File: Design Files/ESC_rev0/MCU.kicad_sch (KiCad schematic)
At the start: 0 parts

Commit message: update2
MCU sch
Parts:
- added C1, C13, C14, C2, C3, C4, C5: C, symbol Device:C
- added C10, C9: 2u2, symbol Device:C
- added C11, C15, C16, C17, C6: 100n, symbol Device:C
- added C12: 1u, symbol Device:C
- added C7: 10u, symbol Device:C
- added C8: 100nF, symbol Device:C
- added D1: LED, symbol Device:LED
- added D2: LED_G, symbol Device:LED
- added D3: LED_R, symbol Device:LED
- added FB1: FerriteBead, symbol Device:FerriteBead
- added J1: Conn_01x06, symbol Connector_Generic:Conn_01x06
- added J2: Conn_01x03, symbol Connector_Generic:Conn_01x03
- added J4: Conn_01x08, symbol Connector_Generic:Conn_01x08
- added R1: 0R, symbol Device:R
- added R10, R7, R8: 2k2, symbol Device:R
- added R2, R3: R, symbol Device:R
- added R4: 1K, symbol Device:R
- added R5, R6: 1k, symbol Device:R
- added R9: 39k, symbol Device:R
- added SW1: SW_DIP_x01, symbol Switch:SW_DIP_x01
- added TH1: 10k, symbol Device:Thermistor_NTC
- added U1: STM32F405RGTx, Package_QFP:LQFP-64_10x10mm_P0.5mm, symbol MCU_ST_STM32F4:STM32F405RGTx
- added Y1: Crystal, symbol Device:Crystal
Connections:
- new net: C13.2, R2.1, Y1.2
- new net: C11.1, C12.1, FB1.1, U1.13 (VDDA)
- new net: D3.2 (A), R6.1
- new net: D2.2 (A), R5.1
- new net: C10.1, U1.31 (VCAP_1)
- new net: J2.3 (Pin_3), R7.2
- new net: R2.2, U1.5 (PH0)
- new net: C14.2, R3.1, Y1.1
- new net: R3.2, U1.6 (PH1)
- new net: D1.2 (A), R4.1
- new net: R1.2, U1.60 (BOOT0)
- new net: C9.1, U1.47 (VCAP_2)
- new net +3V3: C1.1, C16.1, C2.1, C3.1, C4.1, C5.1, C6.1, C7.1, FB1.2, J1.1 (Pin_1), J4.2 (Pin_2), R1.1, R4.2, TH1.1, U1.1 (VBAT), U1.19 (VDD), U1.32 (VDD), U1.48 (VDD), U1.64 (VDD)
- new net +5V: J2.1 (Pin_1), J4.1 (Pin_1)
- new net +VDC: R9.2
- new net ADC_TEMP: R8.2, TH1.2, U1.17 (PA3)
- new net AN_IN: C17.1, R10.2, R9.1, U1.10 (PC2)
- new net BR_S01: U1.27 (PB1)
- new net BR_S02: U1.26 (PB0)
- new net CAN_RX: U1.61 (PB8)
- new net CAN_TX: U1.62 (PB9)
- new net DC_CAL: U1.33 (PB12)
- new net EN_GATE: U1.51 (PC10)
- new net FAULT: U1.53 (PC12)
- new net GND: C1.2, C10.2, C11.2, C12.2, C13.1, C14.1, C15.2, C16.2, C17.2, C2.2, C3.2, C4.2, C5.2, C6.2, C7.2, C8.2, C9.2, D1.1 (K), D2.1 (K), D3.1 (K), J1.3 (Pin_3), J2.2 (Pin_2), J4.3 (Pin_3), J4.8 (Pin_8), R10.1, R8.1, SW1.1, U1.12 (VSSA), U1.18 (VSS), U1.63 (VSS)
- new net H1: U1.43 (PA10)
- new net H2: U1.42 (PA9)
- new net H3: U1.41 (PA8)
- new net HALL_1: U1.58 (PB6)
- new net HALL_2: U1.59 (PB7)
- new net HALL_3: U1.52 (PC11)
- new net L1: U1.36 (PB15)
- new net L2: U1.35 (PB14)
- new net L3: U1.34 (PB13)
- new net LED_GREEN: R5.2, U1.24 (PC4)
- new net LED_RED: R6.2, U1.25 (PC5)
- new net MISO_ADC_EXT2: J4.7 (Pin_7), U1.22 (PA6)
- new net NRST: C8.1, J1.5 (Pin_5), SW1.2, U1.7 (NRST)
- new net RX_SCL_MOSI: J4.6 (Pin_6), U1.23 (PA7), U1.29 (PB10), U1.38 (PC7)
- new net SCK_ADC_EXT: J4.4 (Pin_4), U1.21 (PA5)
- new net SENS1: U1.16 (PA2)
- new net SENS2: U1.15 (PA1)
- new net SENS3: U1.14 (PA0)
- new net SERVO: C15.1, R7.1, U1.57 (PB5)
- new net SWCLK: J1.2 (Pin_2), U1.49 (PA14)
- new net SWDIO: J1.4 (Pin_4), U1.46 (PA13)
- new net TEMP_MOTOR: U1.8 (PC0)
- new net TX_SDA_NSS: J4.5 (Pin_5), U1.20 (PA4), U1.30 (PB11), U1.37 (PC6)
- new net USB_DM: U1.44 (PA11)
- new net USB_DP: U1.45 (PA12)
- no-connect marks 0 -> 13
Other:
- note added: "${TITLE}"
- note added: "100nF decoupling ceramic capacitors"
- note added: "AN_IN = VDC*0.0534 AN_IN = 3.204@60V"
- note added: "COMMUNICATION"
- note added: "NTC"
- note added: "PROGRAMMING / DEBUG"
- note added: "SERVO"
- note added: "Substitute with 100R if used as servo output"
- note added: "VOLTAGE_DIVIDER"
- note added: "internally pulled-up"
- title: (none) -> Microcontroller Unit

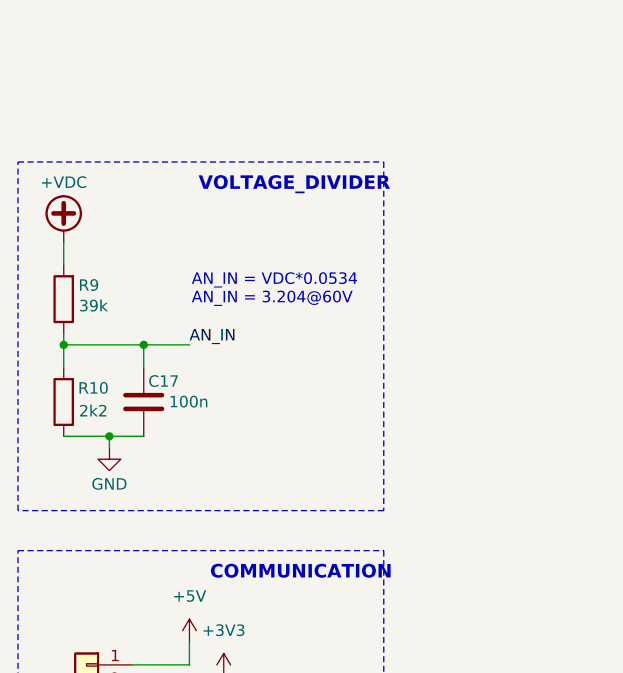
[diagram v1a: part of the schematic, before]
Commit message: update 8
conclusion of mosfets and input protection; can almost concluded
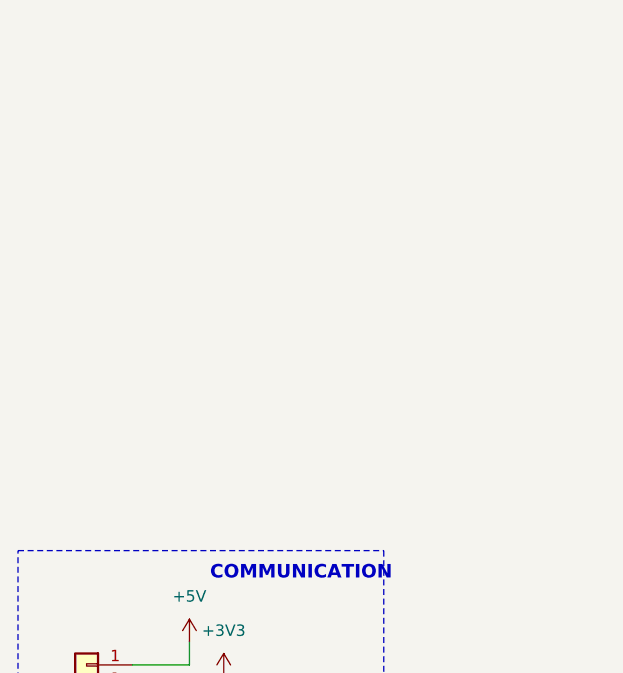
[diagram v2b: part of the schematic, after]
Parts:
- removed C17: 100n, symbol Device:C
- removed R10: 2k2, symbol Device:R
- removed R9: 39k, symbol Device:R
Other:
- note removed: "AN_IN = VDC*0.0534 AN_IN = 3.204@60V"
- note removed: "VOLTAGE_DIVIDER"

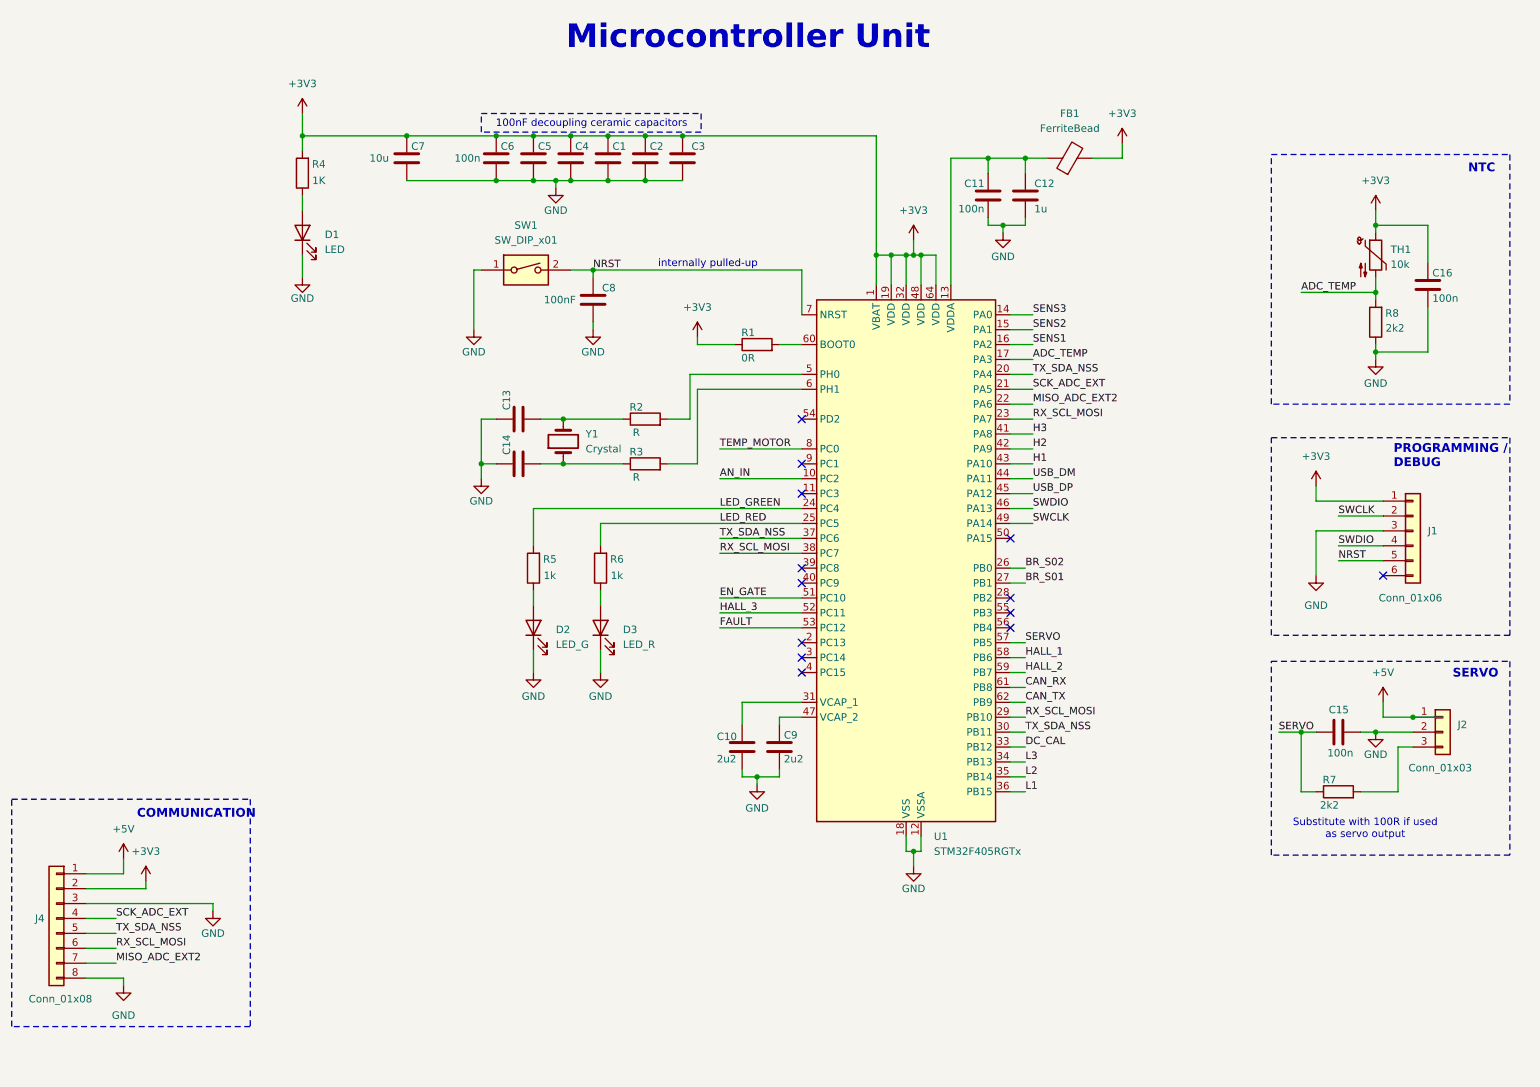
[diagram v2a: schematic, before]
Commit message: update10
modifications to root page, completion of pages step_down and mechanical
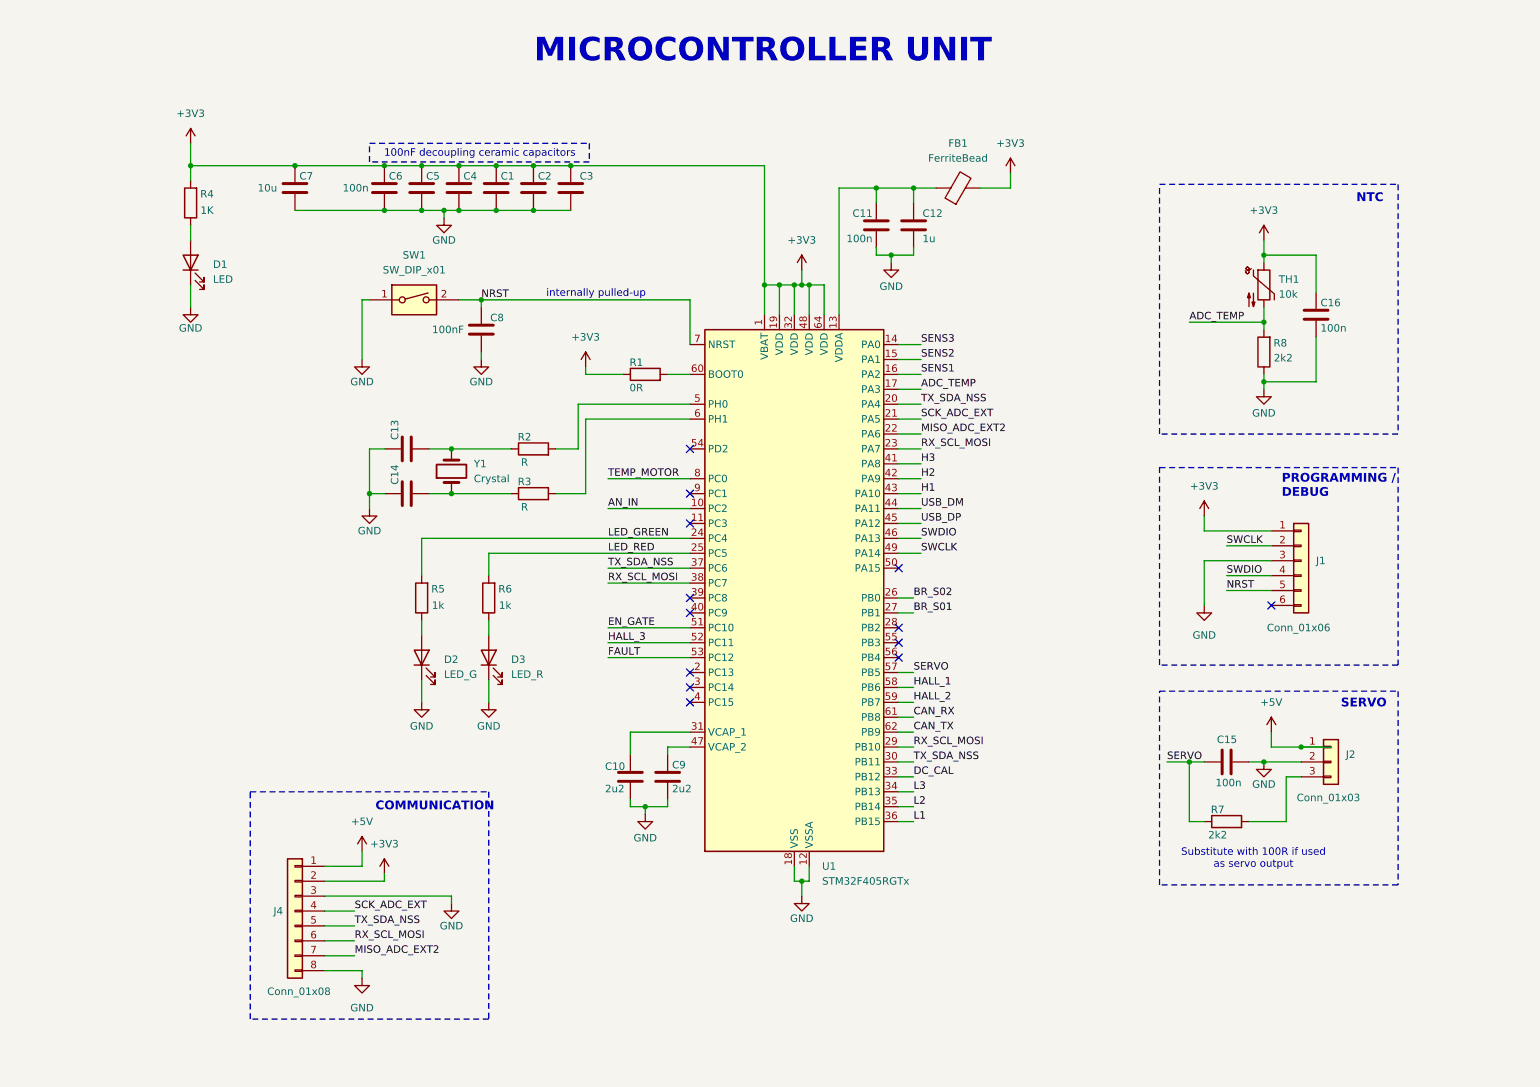
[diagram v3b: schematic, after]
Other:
- title: Microcontroller Unit -> MICROCONTROLLER UNIT
- moved on the sheet: C1, C10, C11, C12, C13, C14, C15, C16, C2, C3, C4, C5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

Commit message: UPDATE 12
started schematics revision: edit and added info and circuits to some pages and assigned some footprints for components
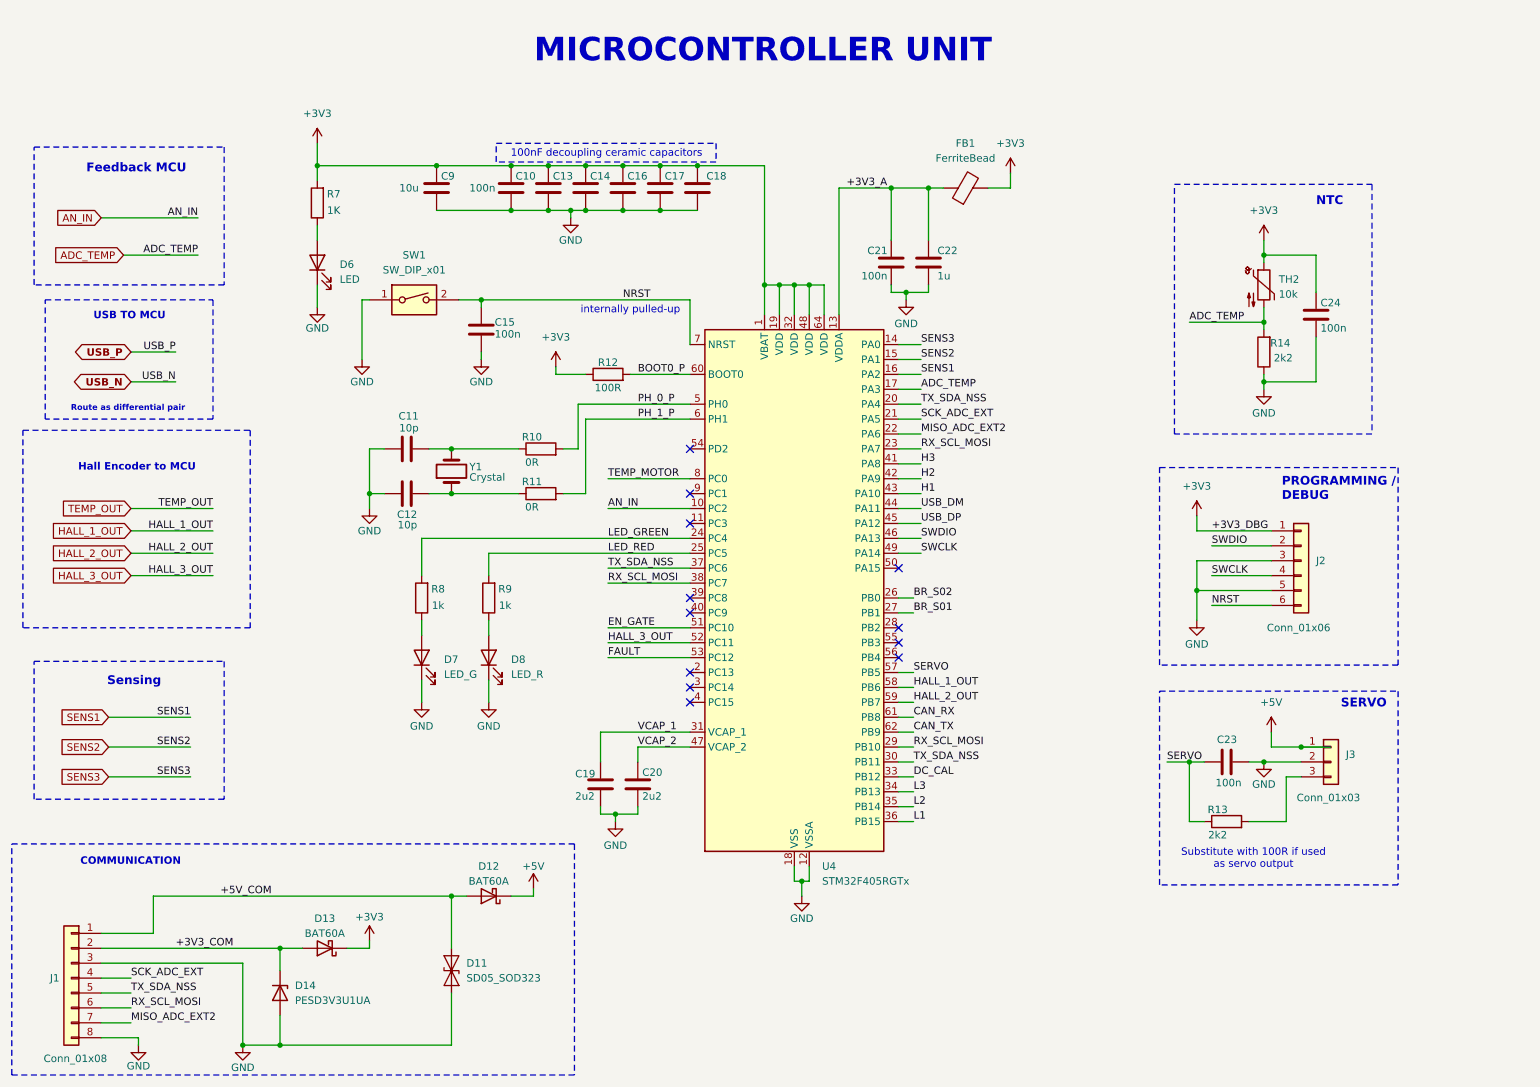
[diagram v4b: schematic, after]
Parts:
- added D11: SD05_SOD323, Diode_SMD:D_SOD-323, symbol Diode:SD05_SOD323
- added D12, D13: BAT60A, Diode_SMD:D_SOD-323, symbol Diode:BAT60A
- added D14: PESD3V3U1UA, Diode_SMD:D_SOD-323F, symbol Diode:PTVS5V0Z1USK
- C10: renamed from C6; footprint (none) -> Capacitor_SMD:C_0201_0603Metric
- C11: renamed from C13; value C -> 10p; footprint (none) -> Capacitor_SMD:C_0201_0603Metric
- C12: renamed from C14; value C -> 10p; footprint (none) -> Capacitor_SMD:C_0201_0603Metric
- C13: renamed from C5; value C -> 100n; footprint (none) -> Capacitor_SMD:C_0201_0603Metric
- C14: renamed from C4; value C -> 100n; footprint (none) -> Capacitor_SMD:C_0201_0603Metric
- C15: renamed from C8; value 100nF -> 100n; footprint (none) -> Capacitor_SMD:C_0201_0603Metric
- C16: renamed from C1; value C -> 100n; footprint (none) -> Capacitor_SMD:C_0201_0603Metric
- C17: renamed from C2; value C -> 100n; footprint (none) -> Capacitor_SMD:C_0201_0603Metric
- C18: renamed from C3; value C -> 100n; footprint (none) -> Capacitor_SMD:C_0201_0603Metric
- C19: renamed from C10; footprint (none) -> Capacitor_SMD:C_0201_0603Metric
- C20: renamed from C9; footprint (none) -> Capacitor_SMD:C_0201_0603Metric
- C21: renamed from C11; footprint (none) -> Capacitor_SMD:C_0201_0603Metric
- C22: renamed from C12; footprint (none) -> Capacitor_SMD:C_0201_0603Metric
- C23: renamed from C15; footprint (none) -> Capacitor_SMD:C_0201_0603Metric
- C24: renamed from C16; footprint (none) -> Capacitor_SMD:C_0201_0603Metric
- C9: renamed from C7; footprint (none) -> Capacitor_SMD:C_0201_0603Metric
- D6: renamed from D1; footprint (none) -> LED_SMD:LED_0201_0603Metric
- D7: renamed from D2; footprint (none) -> LED_SMD:LED_0201_0603Metric
- D8: renamed from D3; footprint (none) -> LED_SMD:LED_0201_0603Metric
- FB1: footprint (none) -> Ferrite_THT:LairdTech_28C0236-0JW-10
- R10: renamed from R2; value R -> 0R
- R11: renamed from R3; value R -> 0R
- R12: renamed from R1; value 0R -> 100R
- renumbered J4 to J1, J1 to J2, J2 to J3, R7 to R13, R8 to R14, R4 to R7, R5 to R8, R6 to R9, TH1 to TH2, U1 to U4
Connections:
- net +3V3: now also D13.1 (K); no longer J1.2 (Pin_2)
- net +5V: now also D12.1 (K); no longer J1.1 (Pin_1)
- net GND: now also J2.5 (Pin_5), D11.1 (A1), D14.2 (A)
- net NRST: now also J2.6 (Pin_6); no longer J2.5 (Pin_5)
- net SWCLK: now also J2.4 (Pin_4); no longer J2.2 (Pin_2)
- net SWDIO: now also J2.2 (Pin_2); no longer J2.4 (Pin_4)
- net +3V3_A: now reaches C21.1, C22.1, FB1.1, U4.13 (VDDA)
- net VCAP_1: now reaches C19.1, U4.31 (VCAP_1)
- net PH_0_P: now reaches R10.2, U4.5 (PH0)
- net PH_1_P: now reaches R11.2, U4.6 (PH1)
- net BOOT0_P: now reaches R12.2, U4.60 (BOOT0)
- net VCAP_2: now reaches C20.1, U4.47 (VCAP_2)
- net HALL_1 renamed HALL_1_OUT
- net HALL_2 renamed HALL_2_OUT
- net HALL_3 renamed HALL_3_OUT
- new net +3V3_COM: D13.2 (A), D14.1 (K), J1.2 (Pin_2)
- new net +5V_COM: D11.2 (A2), D12.2 (A), J1.1 (Pin_1)
- no-connect marks 13 -> 12
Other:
- note added: "Feedback MCU"
- note added: "Hall Encoder to MCU"
- note added: "Route as differential pair"
- note added: "Sensing"
- note added: "USB TO MCU"
- moved on the sheet: C10, C13, C14, C16, C17, C18, C19, C20, C21, C22, C9, D6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
